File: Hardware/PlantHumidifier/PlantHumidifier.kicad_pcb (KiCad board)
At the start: 2 copper layers, 10 parts, among them J1 Conn_01x04_Female, J2 Conn_01x04_Female, J3 Conn_01x05_Female, J4 Conn_01x04_Female, SW1 SW_Push_SPDT, U1 WeMos_D1_mini

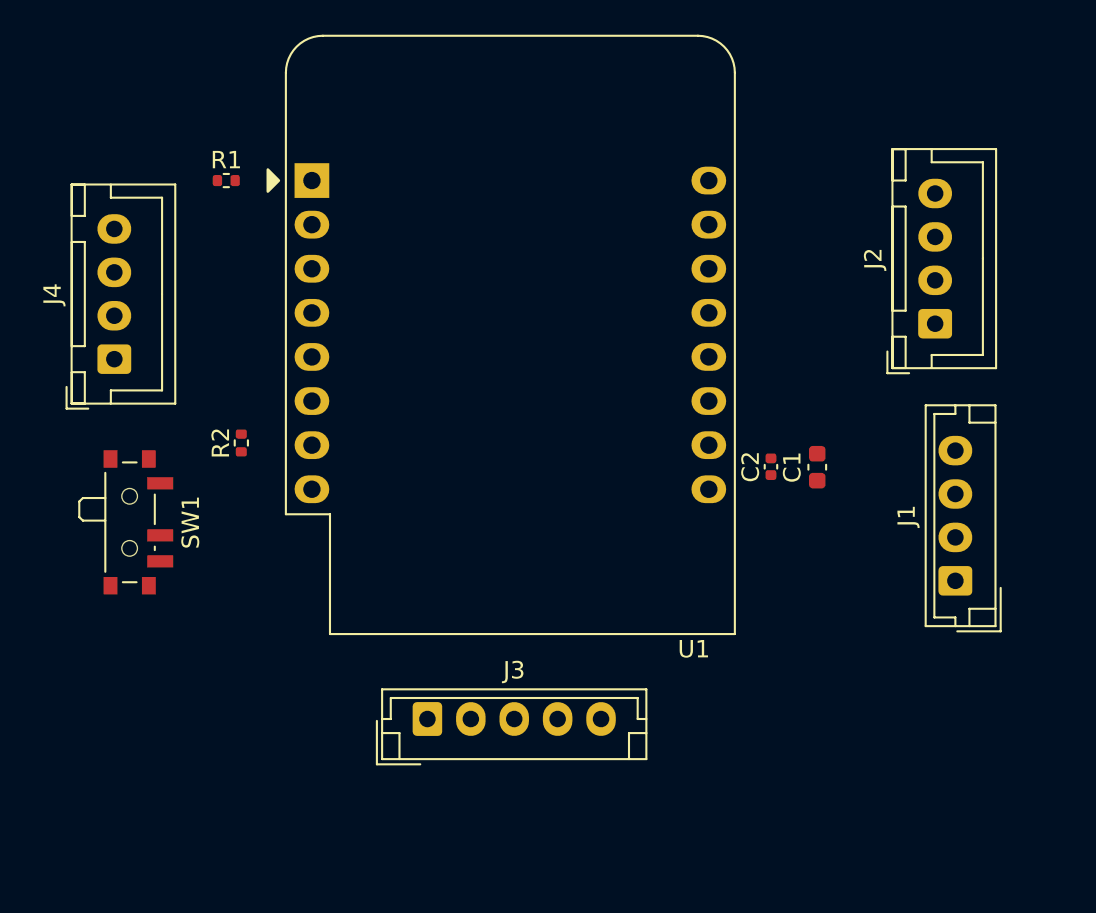
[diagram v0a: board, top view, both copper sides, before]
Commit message: Layout: Update PCB from schematic
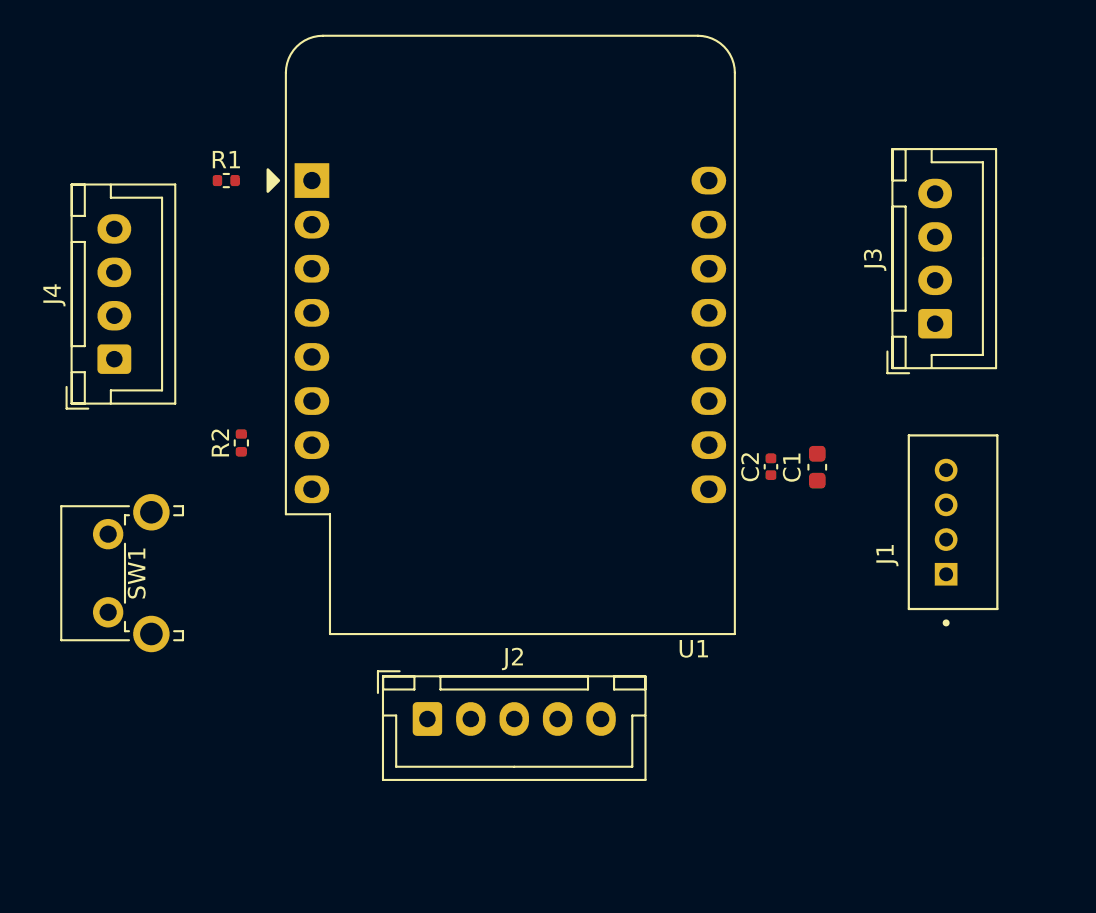
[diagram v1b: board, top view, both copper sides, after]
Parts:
- J1: value Conn_01x04_Female -> 110990030; footprint Connector_JST:JST_EH_B4B-EH-A_1x04_P2.50mm_Vertical -> Seeed_Connectors:SEEED_110990030
- J2: renamed from J3; footprint Connector_JST:JST_EH_B5B-EH-A_1x05_P2.50mm_Vertical -> Connector_JST:JST_XH_B5B-XH-A_1x05_P2.50mm_Vertical
- SW1: value SW_Push_SPDT -> SW_SPST; footprint Button_Switch_SMD:SW_SPDT_PCM12 -> Button_Switch_THT:SW_Tactile_SPST_Angled_PTS645Vx83-2LFS
- moved SW1 5.41 mm to (65.8, 100.4), turned to 90 degrees
- moved J1 3.42 mm to (114.1, 95.2)
- renumbered J2 to J3
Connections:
- SW1 pad 1: +3V3 -> GND

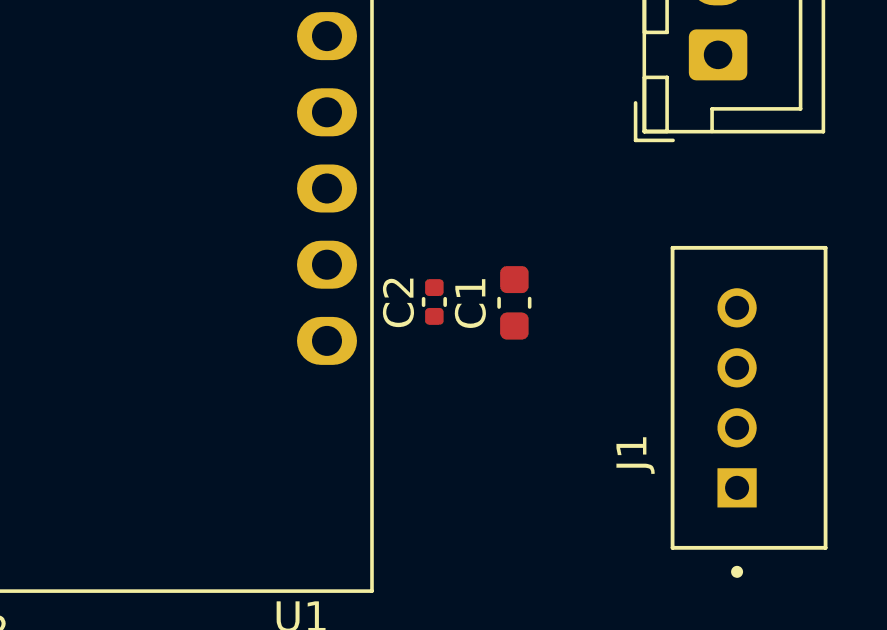
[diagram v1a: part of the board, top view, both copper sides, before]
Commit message: Layout: Add board settings for OSH Park
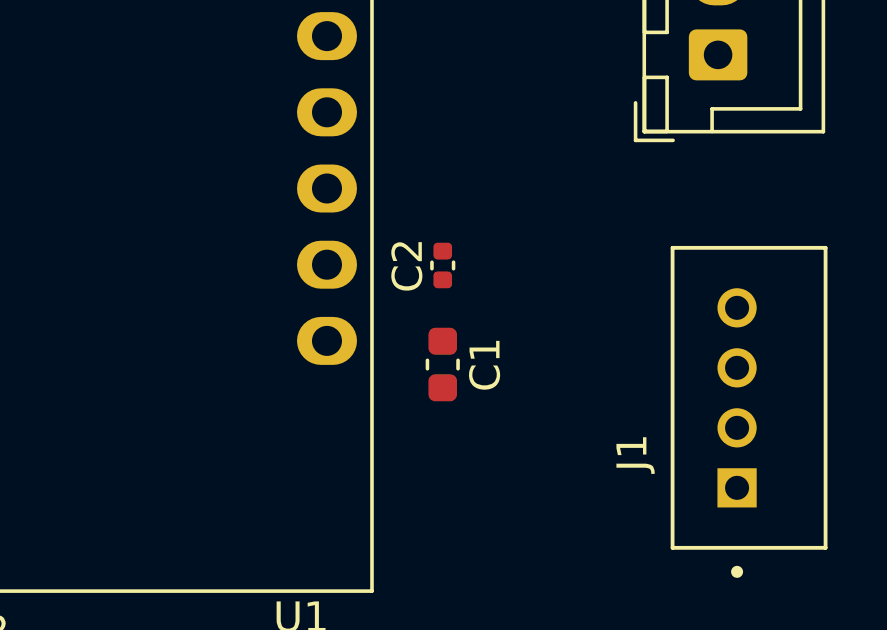
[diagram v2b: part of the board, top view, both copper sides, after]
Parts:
- moved C1 3.15 mm to (104.3, 94.1), turned to -90 degrees
- moved C2 1.25 mm to (104.3, 90.8)
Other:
- rule pad_to_mask_clearance: 0 -> 0.0508
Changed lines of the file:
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@@
   )
   (paper "A4")
+  (title_block
+    (title "Plant Humidifer")
+    (rev "A")
+    (comment 1 "Michael Ly")
+    (comment 2 "Github.com/Michael-Q-Ly")
+  )
   (layers
     (0 "F.Cu" signal)
-    (31 "B.Cu" signal)
+    (31 "B.Cu" power)
     (32 "B.Adhes" user "B.Adhesive")
     (33 "F.Adhes" user "F.Adhesive")
@@
   )
   (setup
-    (pad_to_mask_clearance 0)
+    (stackup
+      (layer "F.SilkS" (type "Top Silk Screen"))
+      (layer "F.Paste" (type "Top Solder Paste"))
+      (layer "F.Mask" (type "Top Solder Mask") (thickness 0.01))
+      (layer "F.Cu" (type "copper") (thickness 0.035))
+      (layer "dielectric 1" (type "core") (thickness 1.51) (material "FR4") (epsilon_r 4.5) (loss_tangent 0.02))
+      (layer "B.Cu" (type "copper") (thickness 0.035))
+      (layer "B.Mask" (type "Bottom Solder Mask") (thickness 0.01))
+      (layer "B.Paste" (type "Bottom Solder Paste"))
+      (layer "B.SilkS" (type "Bottom Silk Screen"))
+      (copper_finish "None")
+      (dielectric_constraints no)
+    )
+    (pad_to_mask_clearance 0.0508)
     (pcbplotparams
       (layerselection 0x00010fc_ffffffff)
@@
   )
   (footprint "Capacitor_SMD:C_0603_1608Metric" (layer "F.Cu")
-    (at 106.68 92.075 90)
+    (at 104.2924 94.1324 -90)
     (descr "Capacitor SMD 0603 (1608 Metric), square (rectangular) end terminal, IPC_7351 nominal, (Body size source: IPC-SM-782 page 76, https://www.pcb-3d.com/wordpress/wp-content/uploads/ipc-sm-782a_amendment_1_and_2.pdf), generated with kicad-footprint-generator")
     (tags "capacitor")
@@
     (fp_line (start 0.8 -0.4) (end 0.8 0.4) (layer "F.Fab") (width 0.1))
     (fp_line (start 0.8 0.4) (end -0.8 0.4) (layer "F.Fab") (width 0.1))
-    (pad "1" smd roundrect (at -0.775 0 90) (size 0.9 0.95) (layers "F.Cu" "F.Paste" "F.Mask") (roundrect_rratio 0.25)
+    (pad "1" smd roundrect (at -0.775 0 270) (size 0.9 0.95) (layers "F.Cu" "F.Paste" "F.Mask") (roundrect_rratio 0.25)
       (net 1 "+5V") (pintype "passive"))
-    (pad "2" smd roundrect (at 0.775 0 90) (size 0.9 0.95) (layers "F.Cu" "F.Paste" "F.Mask") (roundrect_rratio 0.25)
+    (pad "2" smd roundrect (at 0.775 0 270) (size 0.9 0.95) (layers "F.Cu" "F.Paste" "F.Mask") (roundrect_rratio 0.25)
       (net 2 "GND") (pintype "passive"))
     (model "${KICAD6_3DMODEL_DIR}/Capacitor_SMD.3dshapes/C_0603_1608Metric.wrl"
@@
   )
   (footprint "Capacitor_SMD:C_0402_1005Metric" (layer "F.Cu")
-    (at 104.013 92.047 90)
+    (at 104.2924 90.8304 90)
     (descr "Capacitor SMD 0402 (1005 Metric), square (rectangular) end terminal, IPC_7351 nominal, (Body size source: IPC-SM-782 page 76, https://www.pcb-3d.com/wordpress/wp-content/uploads/ipc-sm-782a_amendment_1_and_2.pdf), generated with kicad-footprint-generator")
     (tags "capacitor")

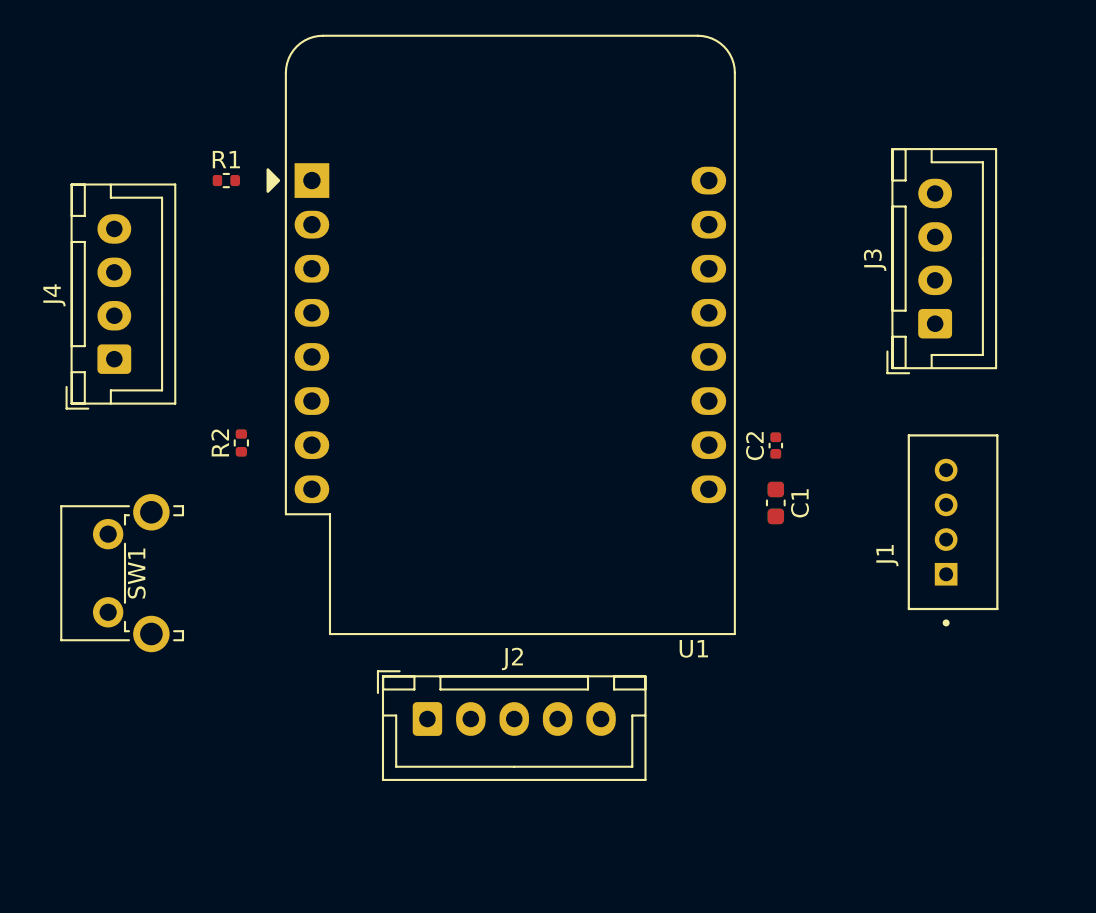
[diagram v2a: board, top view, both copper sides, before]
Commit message: Layout: Route DHT22
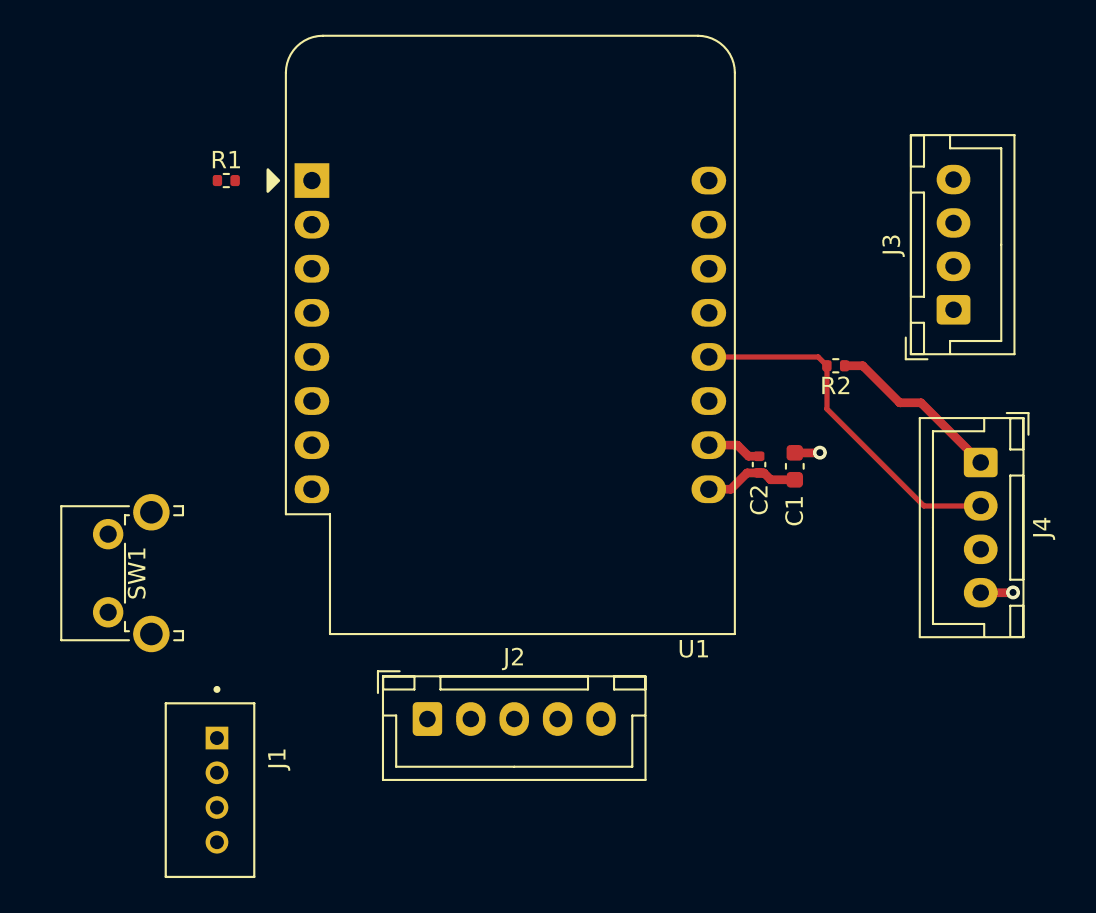
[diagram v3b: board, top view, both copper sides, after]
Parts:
- moved J4 50.3 mm to (116.1, 91.8), turned to -90 degrees
- moved J1 44.7 mm to (72.1, 110.7), turned to -90 degrees
- moved R2 34.5 mm to (107.7, 86.2), turned to 180 degrees
- moved C1 2.37 mm to (105.4, 92.0), turned to 90 degrees
- moved C2 1.46 mm to (103.3, 91.9)
- moved J3 1.33 mm to (114.5, 83.0)
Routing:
- net /DHT22_Sense: track 0.00 -> 20.7 mm
- net +3V3: track 0.00 -> 10.1 mm
- net GND: track 0.00 -> 6.53 mm, vias 0 -> 2
- net +5V: track 0.00 -> 5.51 mm

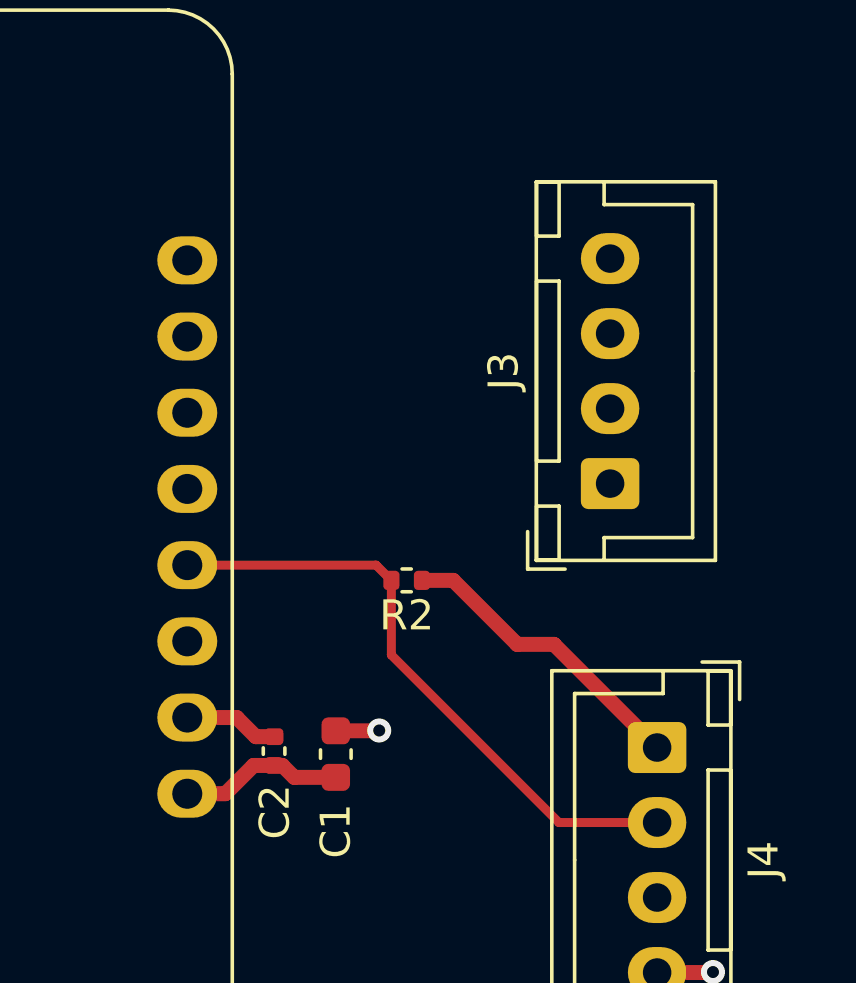
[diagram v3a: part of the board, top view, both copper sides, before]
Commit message: Layout: Route OLED screen
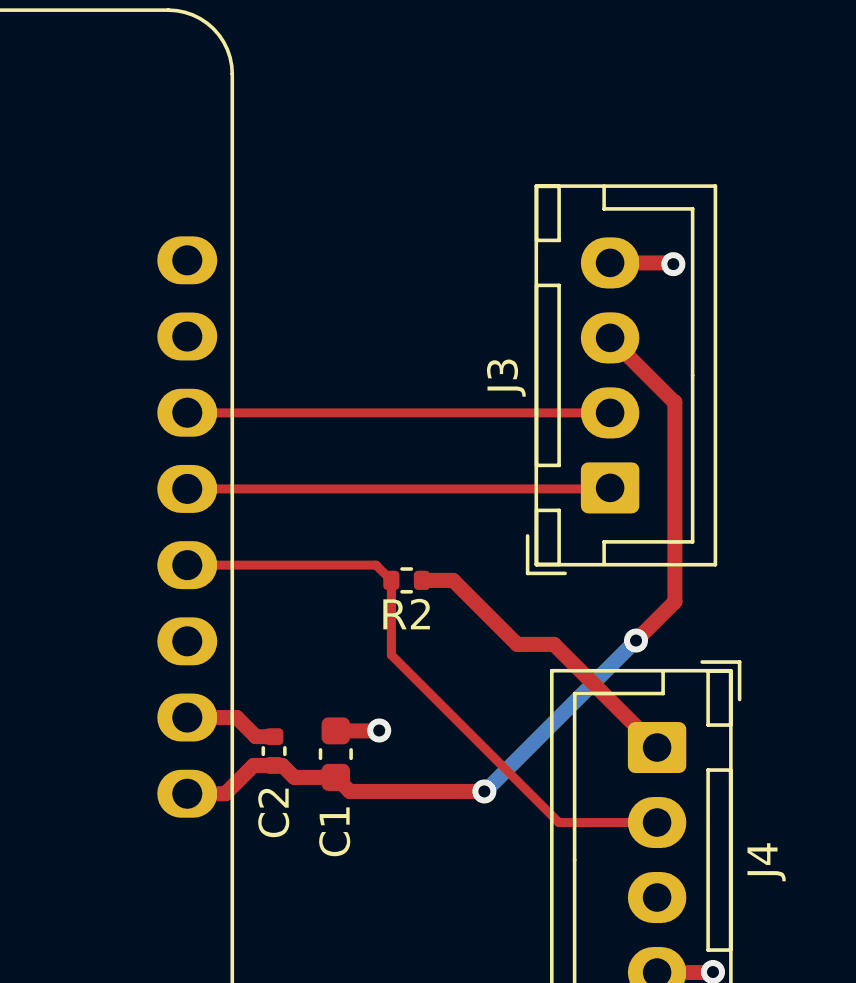
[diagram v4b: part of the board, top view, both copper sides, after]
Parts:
- moved J3 0.14 mm to (114.5, 83.2)
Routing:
- net +5V: track 5.51 -> 29.3 mm, vias 0 -> 2
- net /OLED_SDA: track 0.00 -> 14.1 mm
- net /OLED_SCL: track 0.00 -> 14.1 mm
- net GND: track 6.53 -> 8.66 mm, vias 2 -> 3
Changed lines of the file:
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@@
   )
   (footprint "Connector_JST:JST_XH_B4B-XH-A_1x04_P2.50mm_Vertical" (layer "F.Cu")
-    (at 114.5286 83.0072 90)
+    (at 114.5286 83.1504 90)
     (descr "JST XH series connector, B4B-XH-A (http://www.jst-mfg.com/product/pdf/eng/eXH.pdf), generated with kicad-footprint-generator")
     (tags "connector JST XH vertical")
@@
   )
   (segment (start 103.3272 92.4026) (end 103.604 92.4026) (width 0.5) (layer "F.Cu") (net 1))
+  (segment (start 116.6876 86.9442) (end 115.3922 88.2396) (width 0.5) (layer "F.Cu") (net 1))
+  (segment (start 114.5286 78.1504) (end 116.6676 80.2894) (width 0.5) (layer "F.Cu") (net 1))
+  (segment (start 116.6876 80.2894) (end 116.6876 86.9442) (width 0.5) (layer "F.Cu") (net 1))
   (segment (start 104.0006 92.7992) (end 105.3846 92.7992) (width 0.5) (layer "F.Cu") (net 1))
   (segment (start 103.604 92.4026) (end 104.0006 92.7992) (width 0.5) (layer "F.Cu") (net 1))
   (segment (start 102.644 92.4026) (end 103.3272 92.4026) (width 0.5) (layer "F.Cu") (net 1))
+  (segment (start 116.6676 80.2894) (end 116.6876 80.2894) (width 0.5) (layer "F.Cu") (net 1))
+  (segment (start 110.3376 93.2688) (end 105.8542 93.2688) (width 0.5) (layer "F.Cu") (net 1))
   (segment (start 101.7016 93.345) (end 102.644 92.4026) (width 0.5) (layer "F.Cu") (net 1))
+  (segment (start 105.8542 93.2688) (end 105.3846 92.7992) (width 0.5) (layer "F.Cu") (net 1))
   (segment (start 100.434 93.345) (end 101.7016 93.345) (width 0.5) (layer "F.Cu") (net 1))
+  (via (at 115.3922 88.2396) (size 0.8) (drill 0.4) (layers "F.Cu" "B.Cu") (net 1))
+  (via (at 110.3376 93.2688) (size 0.8) (drill 0.4) (layers "F.Cu" "B.Cu") (net 1))
+  (segment (start 110.363 93.2688) (end 110.3376 93.2688) (width 0.5) (layer "B.Cu") (net 1))
+  (segment (start 115.3922 88.2396) (end 110.363 93.2688) (width 0.5) (layer "B.Cu") (net 1))
   (segment (start 106.82 91.2492) (end 106.8324 91.2368) (width 0.5) (layer "F.Cu") (net 2))
   (segment (start 105.3468 91.2114) (end 105.3846 91.2492) (width 0.5) (layer "F.Cu") (net 2))
   (segment (start 100.434 90.805) (end 102.0826 90.805) (width 0.5) (layer "F.Cu") (net 2))
   (segment (start 105.3846 91.2492) (end 106.82 91.2492) (width 0.5) (layer "F.Cu") (net 2))
+  (segment (start 114.5286 75.6504) (end 116.5952 75.6504) (width 0.5) (layer "F.Cu") (net 2))
+  (segment (start 116.5952 75.6504) (end 116.6368 75.692) (width 0.5) (layer "F.Cu") (net 2))
   (segment (start 116.095 99.3048) (end 117.9414 99.3048) (width 0.5) (layer "F.Cu") (net 2))
   (segment (start 102.0826 90.805) (end 102.7202 91.4426) (width 0.5) (layer "F.Cu") (net 2))
@@
   (segment (start 117.9414 99.3048) (end 117.9576 99.2886) (width 0.5) (layer "F.Cu") (net 2))
   (via (at 117.9576 99.2886) (size 0.8) (drill 0.4) (layers "F.Cu" "B.Cu") (net 2))
+  (via (at 116.6368 75.692) (size 0.8) (drill 0.4) (layers "F.Cu" "B.Cu") (net 2))
   (via (at 106.8324 91.2368) (size 0.8) (drill 0.4) (layers "F.Cu" "B.Cu") (net 2))
+  (segment (start 114.5286 83.1504) (end 114.494 83.185) (width 0.3) (layer "F.Cu") (net 5))
+  (segment (start 114.494 83.185) (end 100.434 83.185) (width 0.3) (layer "F.Cu") (net 5))
+  (segment (start 114.5286 80.6504) (end 100.4394 80.6504) (width 0.3) (layer "F.Cu") (net 6))
+  (segment (start 100.4394 80.6504) (end 100.434 80.645) (width 0.3) (layer "F.Cu") (net 6))
   (segment (start 111.4298 88.3666) (end 109.2962 86.233) (width 0.5) (layer "F.Cu") (net 10))
   (segment (start 116.095 91.8048) (end 112.6568 88.3666) (width 0.5) (layer "F.Cu") (net 10))
